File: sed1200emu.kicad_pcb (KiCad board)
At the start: 2 copper layers, 46.2 x 38.9 mm, 17 parts, among them CN1 PINHD-1X6, CN2 PINHD-1X6, IC1 MEGA8-AI, Q1 CRYSTALHC49S

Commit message: Update Reference Values for BOM
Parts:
- CN1, CN2: value PINHD-1X6 -> Conn_01x06_Pin 2.54mm
- IC1: value MEGA8-AI -> ATMEGA8L-8AU
- Q1: value CRYSTALHC49S -> HC-49/S 16pF
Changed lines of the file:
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@@
         (effects (font (size 1 1) (thickness 0.15)))
     )
-    (fp_text value "MEGA8-AI" (at 0.0843 -1.462526) (layer "F.Fab")
+    (fp_text value "ATMEGA8L-8AU" (at 0.0843 -1.462526) (layer "F.Fab")
         (effects (font (size 1 1) (thickness 0.15)))
     )
@@
         (effects (font (size 1 1) (thickness 0.15)))
     )
-    (fp_text value "PINHD-1X6" (at 0 15.03 90) (layer "F.Fab")
+    (fp_text value "Conn_01x06_Pin 2.54mm" (at 0 15.03 90) (layer "F.Fab")
         (effects (font (size 1 1) (thickness 0.15)))
     )
@@
         (effects (font (size 1 1) (thickness 0.15)))
     )
-    (fp_text value "PINHD-1X6" (at 0 15.03 90) (layer "F.Fab")
+    (fp_text value "Conn_01x06_Pin 2.54mm" (at 0 15.03 90) (layer "F.Fab")
         (effects (font (size 1 1) (thickness 0.15)))
     )
@@
         (effects (font (size 1.143 1.143) (thickness 0.127)) (justify left bottom))
     )
-    (fp_text value "CRYSTALHC49S" (at -5.08 3.937 90) (layer "F.Fab")
+    (fp_text value "HC-49/S 16pF" (at -5.08 3.937 90) (layer "F.Fab")
         (effects (font (size 1.143 1.143) (thickness 0.127)) (justify left bottom))
     )

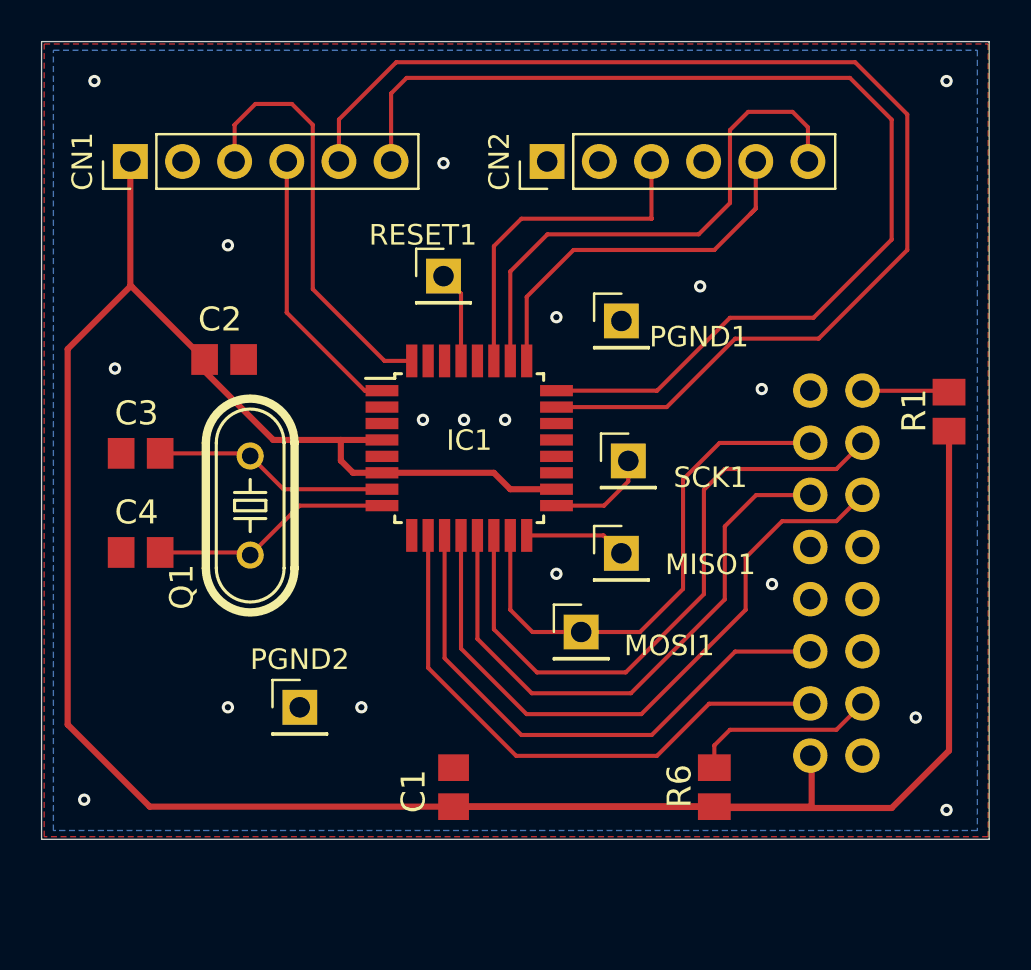
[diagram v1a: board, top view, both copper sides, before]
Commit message: Cleanup PCB, Add UART header, Consolidate SPI headers, Reset VCC Connect
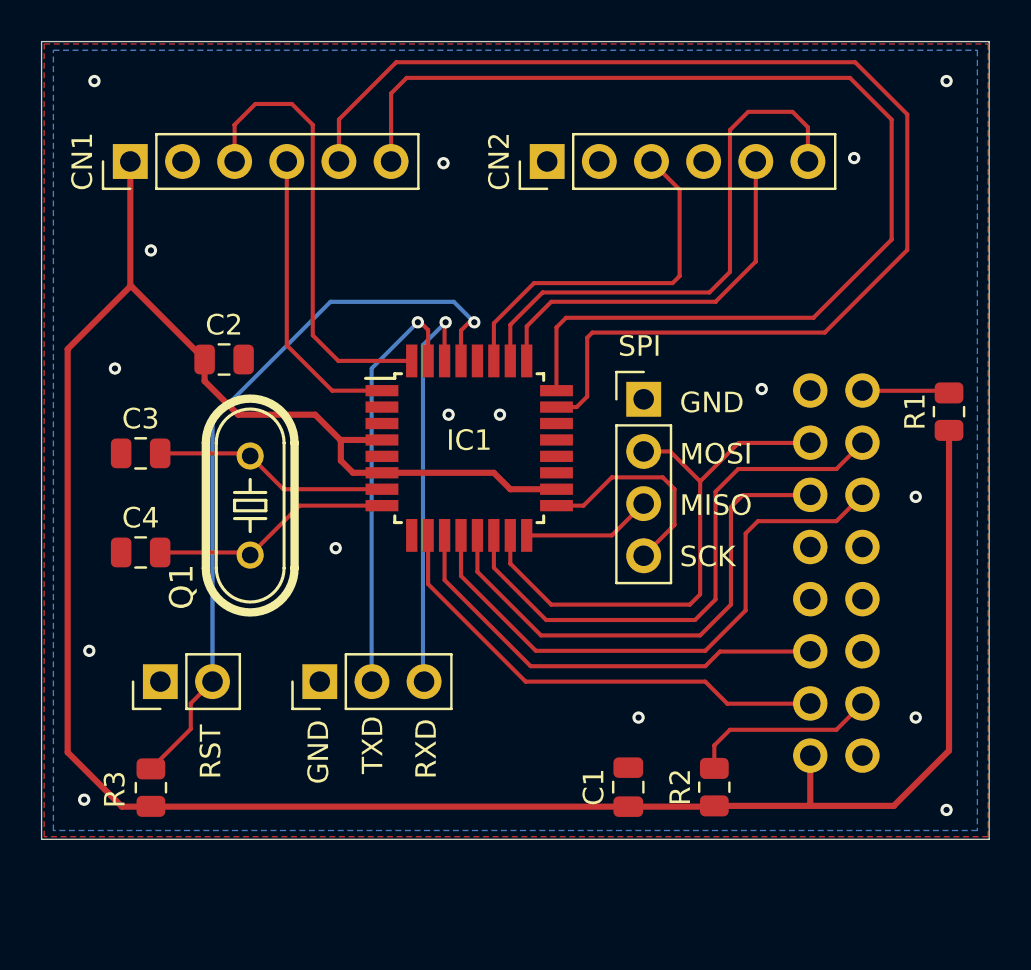
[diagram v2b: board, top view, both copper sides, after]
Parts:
- removed MISO1, MOSI1, PGND1, PGND2, SCK1: Conn_01x01_Pin, Connector_PinHeader_2.54mm:PinHeader_1x01_P2.54mm_Vertical
- added R3: 10k, Resistor_SMD:R_0805_2012Metric, F.Cu at (130.8, 121.9)
- added SPI1: Conn_01x04_Pin, Connector_PinHeader_2.54mm:PinHeader_1x04_P2.54mm_Vertical, F.Cu at (154.8, 103.0)
- added UART1: Conn_01x03_Pin, Connector_PinHeader_2.54mm:PinHeader_1x03_P2.54mm_Vertical, F.Cu at (139.0, 116.8)
- C1, C2: value 0.1 -> 0.1uF; footprint sed1200emu:C0805 -> Capacitor_SMD:C_0805_2012Metric
- C3, C4: footprint sed1200emu:C0805 -> Capacitor_SMD:C_0805_2012Metric
- DIS2: value TUXGR_20X2 -> SMH2002-A
- R1: footprint sed1200emu:M0805 -> Resistor_SMD:R_0805_2012Metric
- R2: renamed from R6; footprint sed1200emu:M0805 -> Resistor_SMD:R_0805_2012Metric
- RESET1: value Conn_01x01_Pin -> Conn_01x02_Pin; footprint Connector_PinHeader_2.54mm:PinHeader_1x01_P2.54mm_Vertical -> Connector_PinHeader_2.54mm:PinHeader_1x02_P2.54mm_Vertical
- moved RESET1 24.1 mm to (131.2, 116.8), turned to 90 degrees
- moved C1 8.51 mm to (154.0, 121.9)
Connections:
- net Net-(DIS2-D4) renamed /ICP
- net Net-(DIS2-D5) renamed /OC1A
- net Net-(DIS2-D6) renamed /OC1B
- net Net-(DIS2-D7) renamed /MOSI
- net Net-(DIS2-E) renamed /AIN1
- net Net-(DIS2-RS) renamed /AIN0
- net Net-(IC1-PC0(ADC0)) renamed /ADC0
- net Net-(IC1-PC1(ADC1)) renamed /ADC1
- net Net-(IC1-PC2(ADC2)) renamed /ADC2
- net Net-(IC1-PC3(ADC3)) renamed /ADC3
- net Net-(IC1-PC4(ADC4/SDA)) renamed /ADC4
- net Net-(IC1-PD2(INT0)) renamed /INT0
- net Net-(IC1-PD3(INT1)) renamed /INT1
- IC1 pad 16: Net-(IC1-PB4(MISO)) -> /MISO
- IC1 pad 17: Net-(IC1-PB5(SCK)) -> /SCK
- IC1 pad 30: unconnected-(IC1-PD0(RXD)-Pad30) -> /RXD
- IC1 pad 31: unconnected-(IC1-PD1(TXD)-Pad31) -> /TXD
- RESET1 pad 1: Net-(IC1-PC6(/RESET)) -> GND
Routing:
- net Net-(IC1-PC6(/RESET)): track 4.48 -> 36.1 mm, vias 0 -> 1
- net /TXD: track 0.00 -> 20.6 mm, vias 0 -> 1
- net /RXD: track 0.00 -> 19.9 mm, vias 0 -> 1
- net VCC: track 137.7 -> 121.3 mm
- net /SCK: track 0.00 -> 10.4 mm
- net /MISO: track 0.00 -> 6.34 mm
- net /AIN1: track 27.0 -> 22.0 mm
- net Net-(IC1-PB5(SCK)): track 4.99 -> 0.00 mm
- net Net-(IC1-PB4(MISO)): track 4.97 -> 0.00 mm
- net /AIN0: track 27.9 -> 23.4 mm
- net /ICP: track 32.3 -> 28.4 mm
- net /OC1B: track 31.0 -> 27.2 mm
- net /OC1A: track 28.4 -> 24.9 mm
- net /ADC1: track 54.1 -> 55.9 mm
- net /ADC0: track 58.8 -> 60.5 mm
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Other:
- board text added: "GND"
- board text added: "MISO"
- board text added: "MOSI"
- board text added: "RST"
- board text added: "RXD"
- board text added: "SCK"
- board text added: "SPI"
- board text added: "TXD"

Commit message: Cleanup edge cuts and fill zones
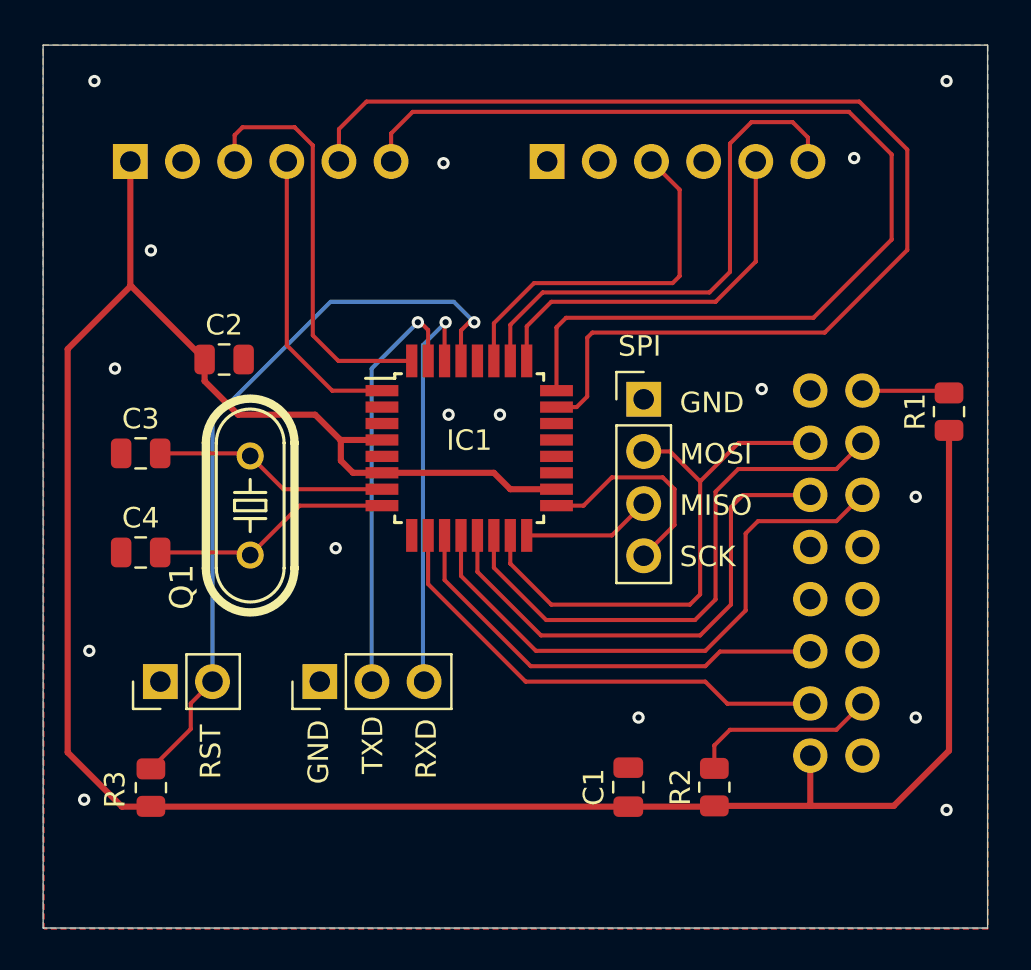
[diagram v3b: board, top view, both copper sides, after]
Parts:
- CN1, CN2: moved to B.Cu
- turned CN1 to -90 degrees
- turned CN2 to -90 degrees
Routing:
- net /ADC1: track 55.9 -> 52.4 mm
- net /ADC0: track 60.5 -> 57.6 mm
- net /INT0: track 22.0 -> 20.2 mm
- net /ADC3: track 26.6 -> 25.5 mm
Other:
- board size 46.2 x 38.9 mm -> 46 x 43 mm
